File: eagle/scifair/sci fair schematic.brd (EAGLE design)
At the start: 45.4 x 80 mm, 16 parts, among them IC1 LM555N, IC2 LM340H-12, Q1 BC817-16W, Q2 BC817-16W

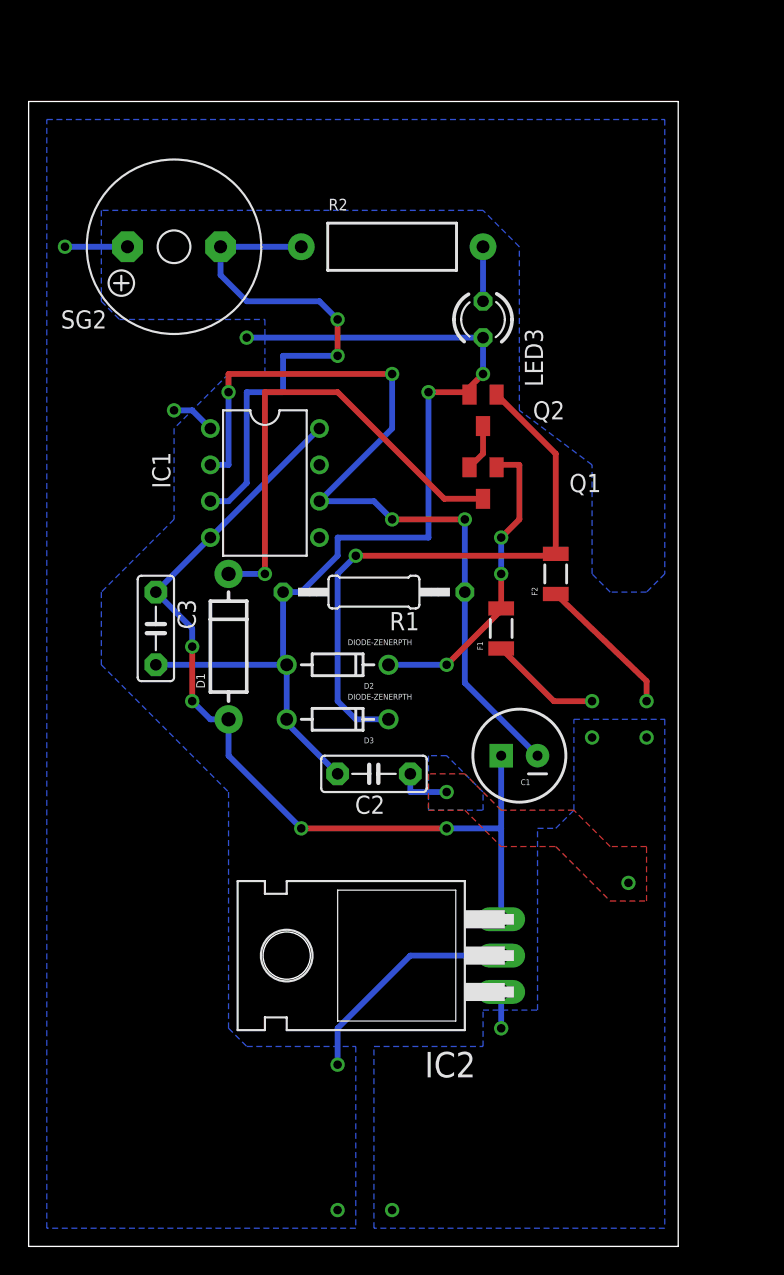
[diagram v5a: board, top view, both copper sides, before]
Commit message: Start work on cost reduction, including eliminating SMD componenents (whose S&H were very high)
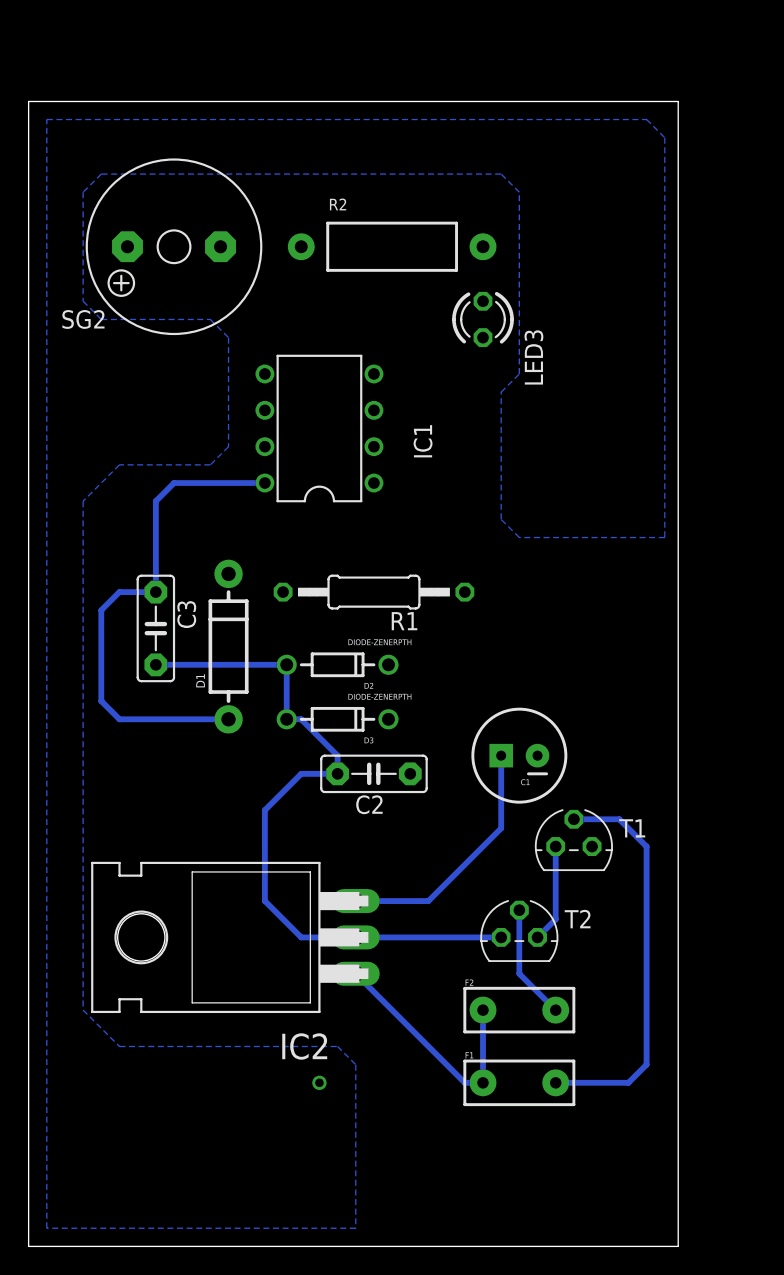
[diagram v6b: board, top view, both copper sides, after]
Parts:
- removed Q1, Q2: BC817-16W, semicon-smd-ipc:SOT23
- added T1, T2: 2N3565, transistor:TO92
- F1, F2: value PTCSMD -> PTCPTH; device SparkFun-PowerIC:PTC-1206 -> SparkFun-PowerIC:PTC
- moved F1 31.8 mm to (91.4, 12.7), turned to 0 degrees
- moved F2 30.6 mm to (91.4, 17.8), turned to 0 degrees
- moved IC2 10.2 mm to (69.8, 22.9)
- moved IC1 5.39 mm to (77.5, 58.4), turned to 90 degrees
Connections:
- net GND: now also T2.3; no longer Q2.2
- net N$4: now also T1.3, T2.1; no longer Q1.2, Q2.3
- net N$7: now also T1.1; no longer Q1.3
- net N$8: now also F1.P$2, T1.2; no longer F1.2, Q1.1
- net N$9: now also F2.P$2, T2.2; no longer F2.2, Q2.1
- net VCC: now also F1.P$1, F2.P$1; no longer F1.1, F2.1
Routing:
- net N$11: track 59.3 -> 0.00 mm, vias 4 -> 0
- net GND: track 93.4 -> 48.9 mm, vias 7 -> 1
- net N$10: track 37.9 -> 0.00 mm, vias 2 -> 0
- net N$9: track 41.6 -> 8.04 mm, vias 1 -> 0
- net N$7: track 33.6 -> 0.00 mm, vias 1 -> 0
- net 5V: track 63.0 -> 51.9 mm, vias 4 -> 0
- net VCC: track 24.4 -> 17.1 mm, vias 8 -> 0
- net N$8: track 21.8 -> 28.0 mm, vias 3 -> 0
- net N$12: track 3.81 -> 0.00 mm
- net N$4: track 3.27 -> 6.88 mm
- removed copper zone on layer 1, net VCC
- removed copper zone on layer 16, net VCC

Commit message: Finalize cost-reduction design
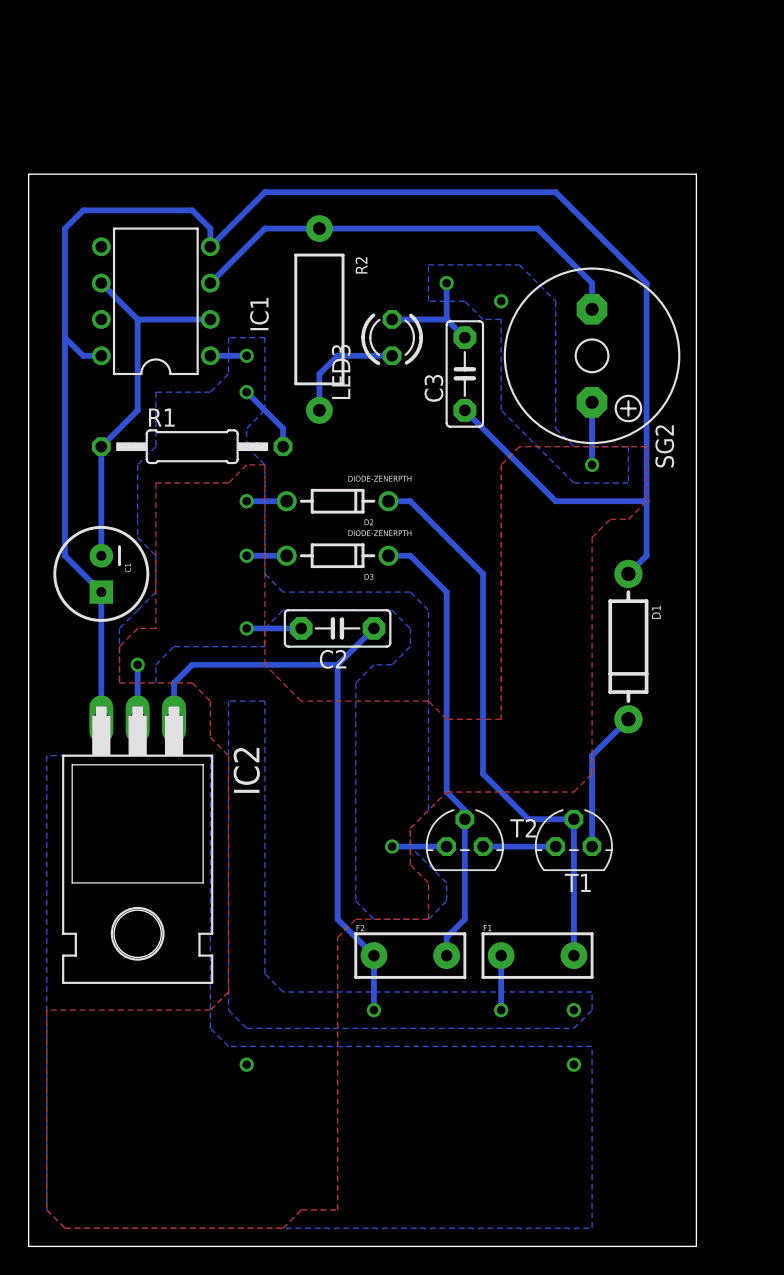
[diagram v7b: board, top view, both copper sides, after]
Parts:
- moved C1 31.9 mm to (62.2, 48.3), turned to 270 degrees
- moved SG2 30.2 mm to (96.5, 63.5), turned to 270 degrees
- moved C3 28.0 mm to (87.6, 62.2), turned to 90 degrees
- moved D1 27.9 mm to (99.1, 43.2), turned to 270 degrees
- moved R1 16.3 mm to (68.6, 57.1), turned to 0 degrees
- moved IC1 14.5 mm to (66.0, 67.3)
- moved D2 11.4 mm to (78.7, 53.3)
- moved D3 11.4 mm to (78.7, 49.5)
- moved C2 10.5 mm to (78.7, 44.5)
- moved F1 8.98 mm to (92.7, 21.6)
- moved F2 8.52 mm to (83.8, 21.6)
- moved T2 7.41 mm to (87.6, 29.2)
- moved IC2 7.18 mm to (64.8, 27.9), turned to 180 degrees
- moved R2 7.18 mm to (77.5, 66.0), turned to 270 degrees
- moved LED3 6.48 mm to (82.5, 64.8), turned to 90 degrees
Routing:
- net 5V: track 51.9 -> 121.8 mm
- net N$10: track 0.00 -> 31.7 mm
- net VCC: track 17.1 -> 47.1 mm, vias 0 -> 3
- net N$11: track 0.00 -> 26.2 mm
- net N$9: track 8.04 -> 31.6 mm
- net GND: track 48.9 -> 36.9 mm, vias 1 -> 12
- net N$8: track 28.0 -> 39.9 mm
- net N$7: track 0.00 -> 9.94 mm
- net N$12: track 0.00 -> 8.15 mm
- net N$4: track 6.88 -> 5.08 mm
- added copper zone on layer 1, net GND
- added copper zone on layer 16, net VCC
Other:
- board size 45.4 x 80 mm -> 46.7 x 74.9 mm

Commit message: Fix potential via clearance problem in top-layer GND pour
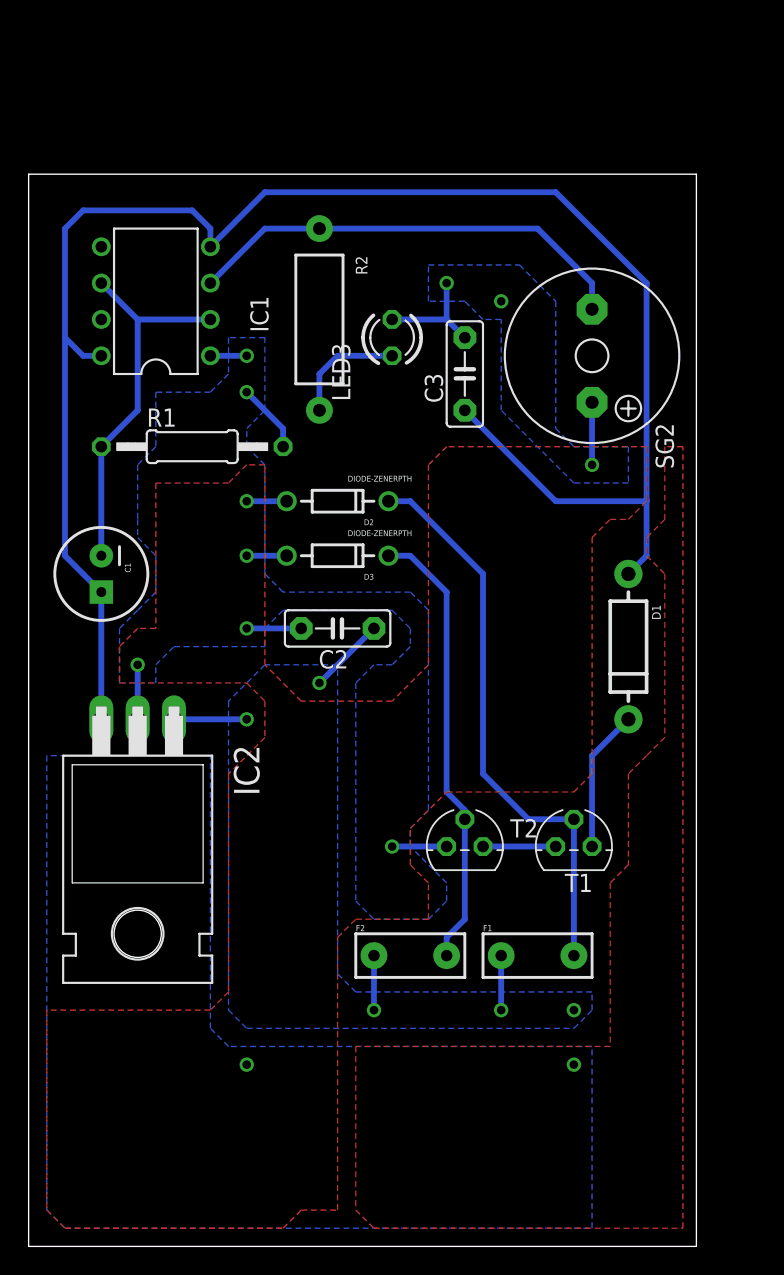
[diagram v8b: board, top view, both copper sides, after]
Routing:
- net VCC: track 47.1 -> 18.1 mm, vias 3 -> 5
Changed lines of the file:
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@@
 <vertex x="100.33" y="53.34"/>
 <vertex x="100.33" y="57.15"/>
-<vertex x="91.44" y="57.15"/>
-<vertex x="90.17" y="55.88"/>
-<vertex x="90.17" y="38.1"/>
-<vertex x="86.36" y="38.1"/>
-<vertex x="85.09" y="39.37"/>
+<vertex x="86.36" y="57.15"/>
+<vertex x="85.09" y="55.88"/>
+<vertex x="85.09" y="41.91"/>
+<vertex x="82.55" y="39.37"/>
 <vertex x="76.2" y="39.37"/>
 <vertex x="73.66" y="41.91"/>
@@
 <vertex x="63.5" y="43.18"/>
 <vertex x="63.5" y="40.64"/>
-<vertex x="68.58" y="40.64"/>
-<vertex x="69.85" y="39.37"/>
-<vertex x="69.85" y="36.83"/>
-<vertex x="71.12" y="35.56"/>
+<vertex x="72.39" y="40.64"/>
+<vertex x="73.66" y="39.37"/>
+<vertex x="73.66" y="36.83"/>
+<vertex x="71.12" y="34.29"/>
 <vertex x="71.12" y="19.05"/>
 <vertex x="69.85" y="17.78"/>
@@
 <via x="95.25" y="13.97" extent="1-16" drill="0.6" shape="square"/>
 <wire x1="64.77" y1="38.1" x2="64.77" y2="41.91" width="0.4064" layer="16"/>
+<polygon width="0.4064" layer="1">
+<vertex x="80.01" y="3.81"/>
+<vertex x="81.28" y="2.54"/>
+<vertex x="102.87" y="2.54"/>
+<vertex x="102.87" y="57.15"/>
+<vertex x="101.6" y="57.15"/>
+<vertex x="101.6" y="52.07"/>
+<vertex x="100.33" y="50.8"/>
+<vertex x="100.33" y="49.53"/>
+<vertex x="101.6" y="48.26"/>
+<vertex x="101.6" y="36.83"/>
+<vertex x="100.33" y="35.56"/>
+<vertex x="99.06" y="34.29"/>
+<vertex x="99.06" y="27.94"/>
+<vertex x="97.79" y="26.67"/>
+<vertex x="97.79" y="15.24"/>
+<vertex x="80.01" y="15.24"/>
+</polygon>
 </signal>
 <signal name="5V">
@@
 <contactref element="F1" pad="P$1"/>
 <contactref element="F2" pad="P$1"/>
-<wire x1="67.31" y1="38.1" x2="67.31" y2="40.64" width="0.4064" layer="16"/>
-<wire x1="67.31" y1="40.64" x2="68.58" y2="41.91" width="0.4064" layer="16"/>
-<wire x1="68.58" y1="41.91" x2="78.74" y2="41.91" width="0.4064" layer="16"/>
-<wire x1="78.74" y1="41.91" x2="81.28" y2="44.45" width="0.4064" layer="16"/>
 <polygon width="0.4064" layer="16">
 <vertex x="71.12" y="39.37"/>
@@
 <vertex x="96.52" y="17.78"/>
 <vertex x="96.52" y="19.05"/>
-<vertex x="74.93" y="19.05"/>
-<vertex x="73.66" y="20.32"/>
-<vertex x="73.66" y="39.37"/>
+<vertex x="80.01" y="19.05"/>
+<vertex x="78.74" y="20.32"/>
+<vertex x="78.74" y="41.91"/>
+<vertex x="73.66" y="41.91"/>
 </polygon>
 <via x="81.28" y="17.78" extent="1-16" drill="0.6" shape="square"/>
@@
 <wire x1="81.28" y1="17.78" x2="81.28" y2="21.59" width="0.4064" layer="16"/>
 <wire x1="90.17" y1="17.78" x2="90.17" y2="21.59" width="0.4064" layer="16"/>
-<wire x1="81.28" y1="21.59" x2="78.74" y2="24.13" width="0.4064" layer="16"/>
-<wire x1="78.74" y1="24.13" x2="78.74" y2="41.91" width="0.4064" layer="16"/>
 <via x="95.25" y="17.78" extent="1-16" drill="0.6" shape="square"/>
+<via x="72.39" y="38.1" extent="1-16" drill="0.6" shape="square"/>
+<wire x1="72.39" y1="38.1" x2="67.31" y2="38.1" width="0.4064" layer="16"/>
+<via x="77.47" y="40.64" extent="1-16" drill="0.6" shape="square"/>
+<wire x1="77.47" y1="40.64" x2="81.28" y2="44.45" width="0.4064" layer="16"/>
 </signal>
 <signal name="N$4">
